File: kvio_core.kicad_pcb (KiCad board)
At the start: 6 copper layers, 60 x 41 mm, 196 parts, among them J1001 16-pin_FFC_(SFV16R), J1101 16-pin_FFC_(SFV16R), J1301 USB3_B_Micro, J401 16-pin_FFC_(SFV16R), J501 16-pin_FFC_(SFV16R), J601 16-pin_FFC_(SFV16R), J701 16-pin_FFC_(SFV16R), J801 16-pin_FFC_(SFV16R), J901 16-pin_FFC_(SFV16R), U1001 EMI8143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

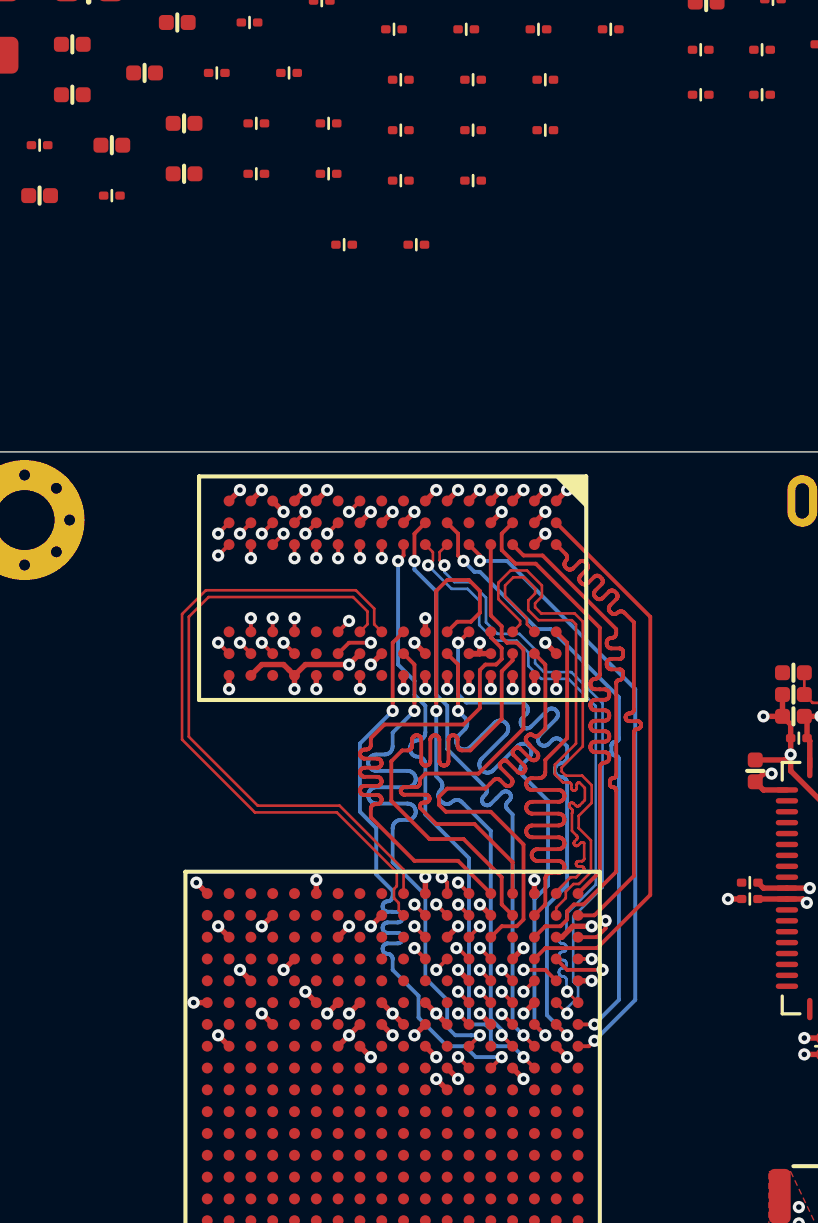
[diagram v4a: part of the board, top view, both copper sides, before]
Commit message: Cleaning up length tuning
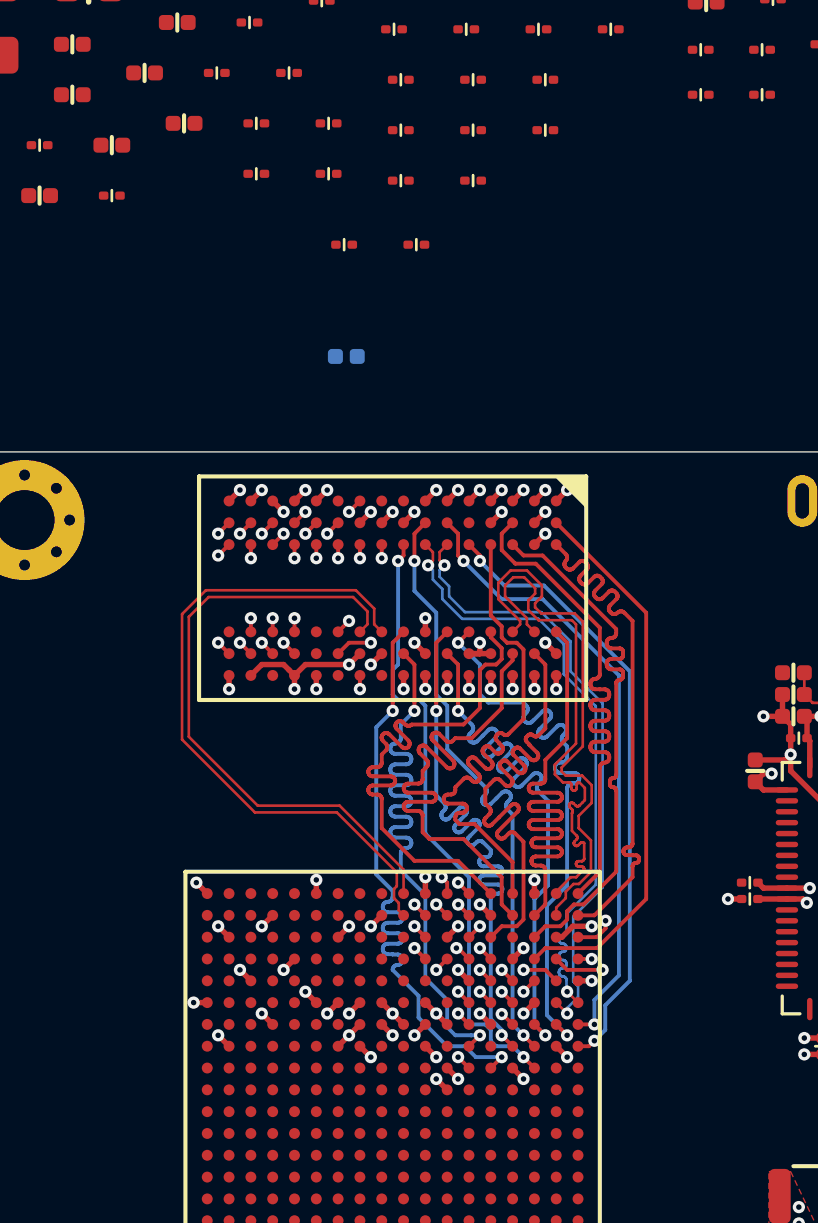
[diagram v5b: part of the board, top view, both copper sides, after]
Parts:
- C217: moved to B.Cu
- moved C217 8.96 mm to (183.3, 85.5)

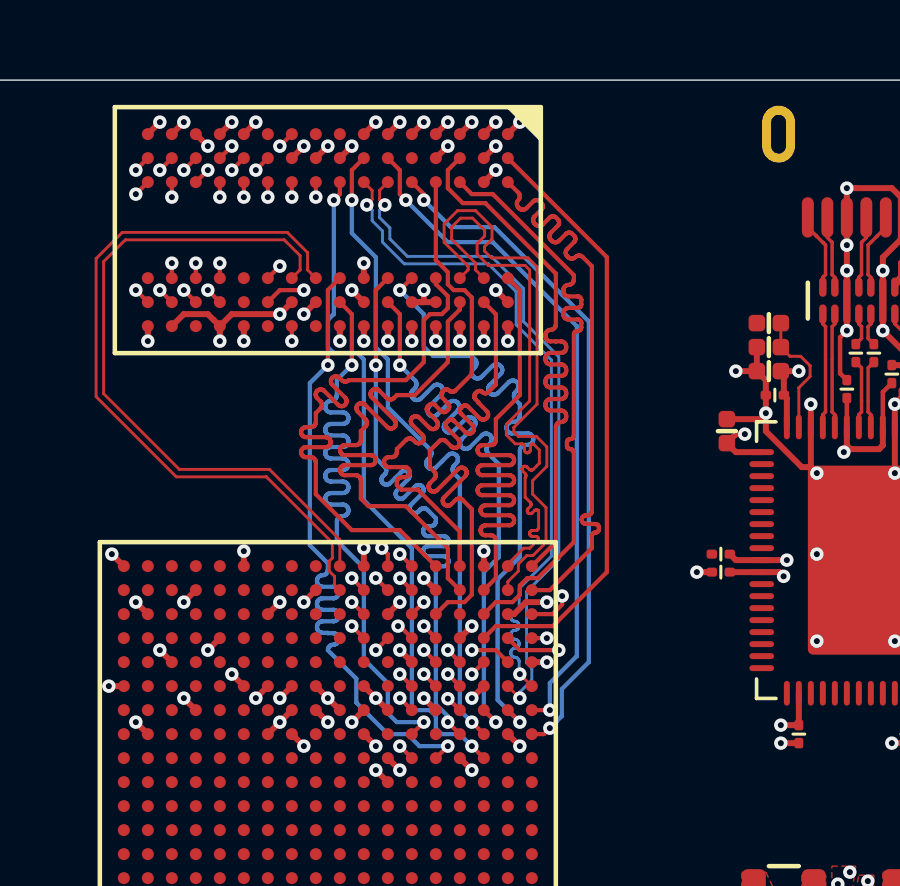
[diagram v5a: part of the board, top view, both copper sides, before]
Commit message: Fixing for adding pad lengths
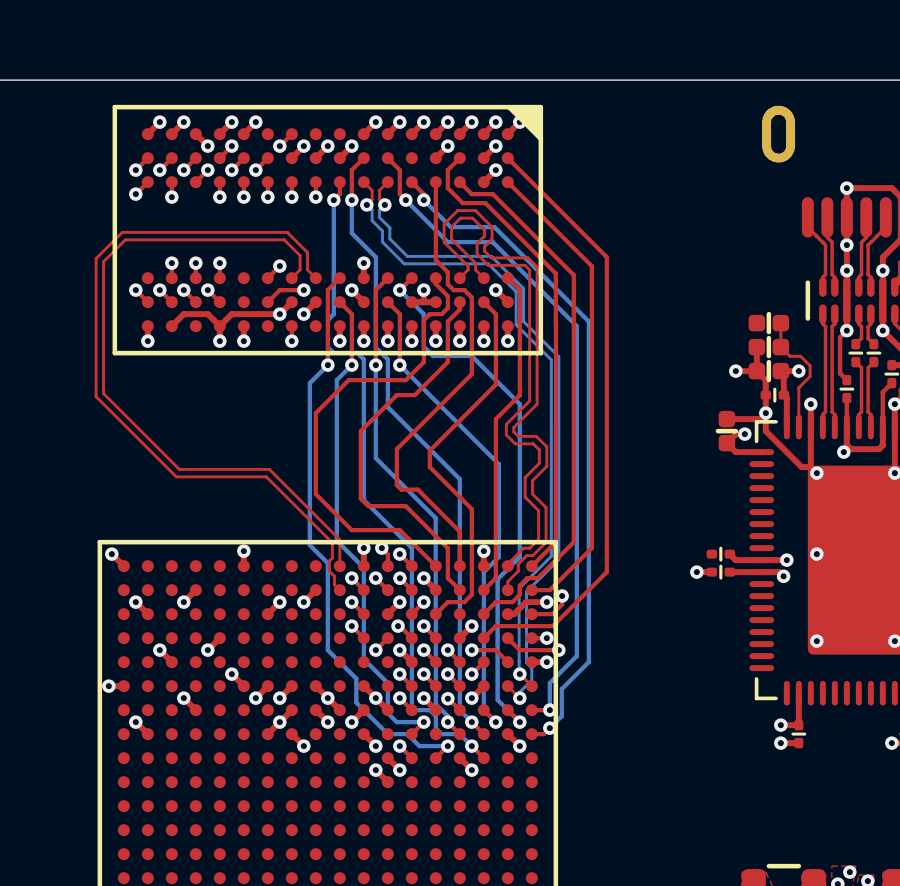
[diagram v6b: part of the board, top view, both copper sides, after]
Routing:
- net /DDR Memory/A4: track 26.2 -> 14.0 mm
- net /DDR Memory/BA1: track 26.2 -> 14.3 mm
- net /DDR Memory/A6: track 26.2 -> 15.8 mm
- net /DDR Memory/A1: track 26.2 -> 16.9 mm
- net /DDR Memory/DQ12: track 20.2 -> 11.1 mm
- net /DDR Memory/DQ14: track 20.2 -> 12.9 mm
- net /DDR Memory/A12: track 26.1 -> 19.2 mm
- net /DDR Memory/DQ10: track 20.2 -> 13.4 mm
- net /DDR Memory/A11: track 26.1 -> 20.0 mm
- net /DDR Memory/DQ3: track 22.6 -> 16.5 mm
- net /DDR Memory/DQ1: track 22.6 -> 16.5 mm
- net /DDR Memory/DQ5: track 22.6 -> 16.7 mm
- net /DDR Memory/A10: track 26.2 -> 21.5 mm
- net /DDR Memory/DQ8: track 20.2 -> 15.5 mm
- net /DDR Memory/UDM: track 20.2 -> 15.7 mm
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
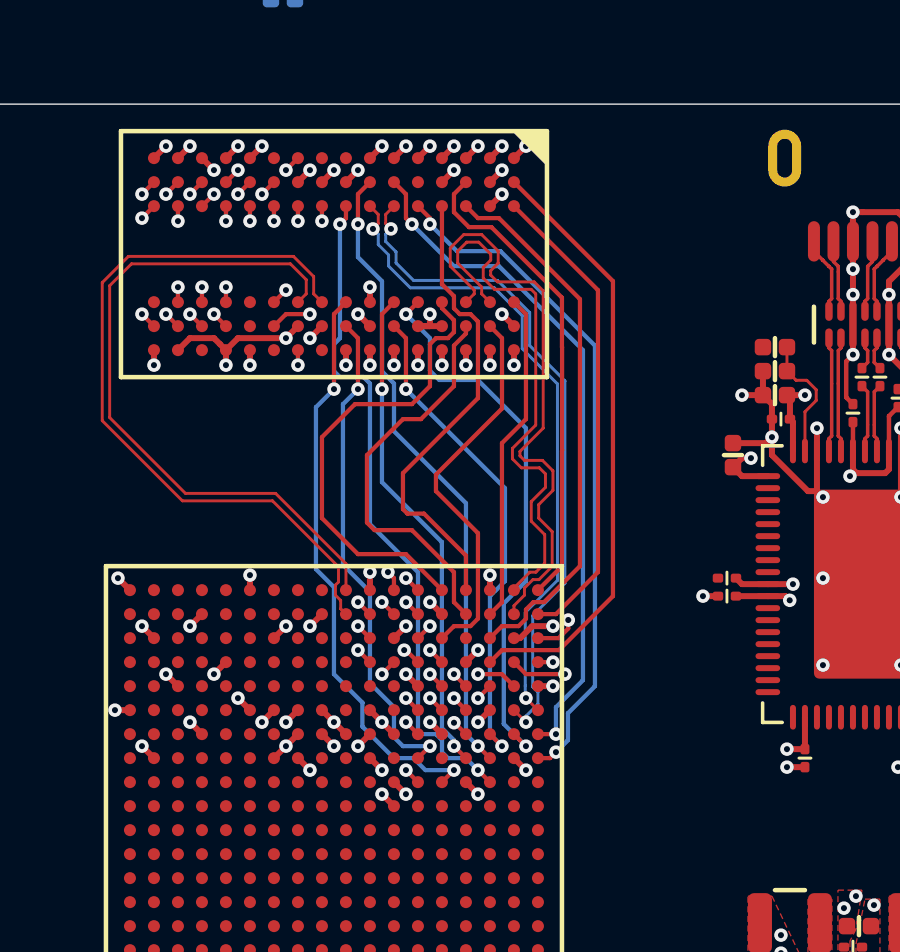
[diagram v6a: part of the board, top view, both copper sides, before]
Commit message: New length matching
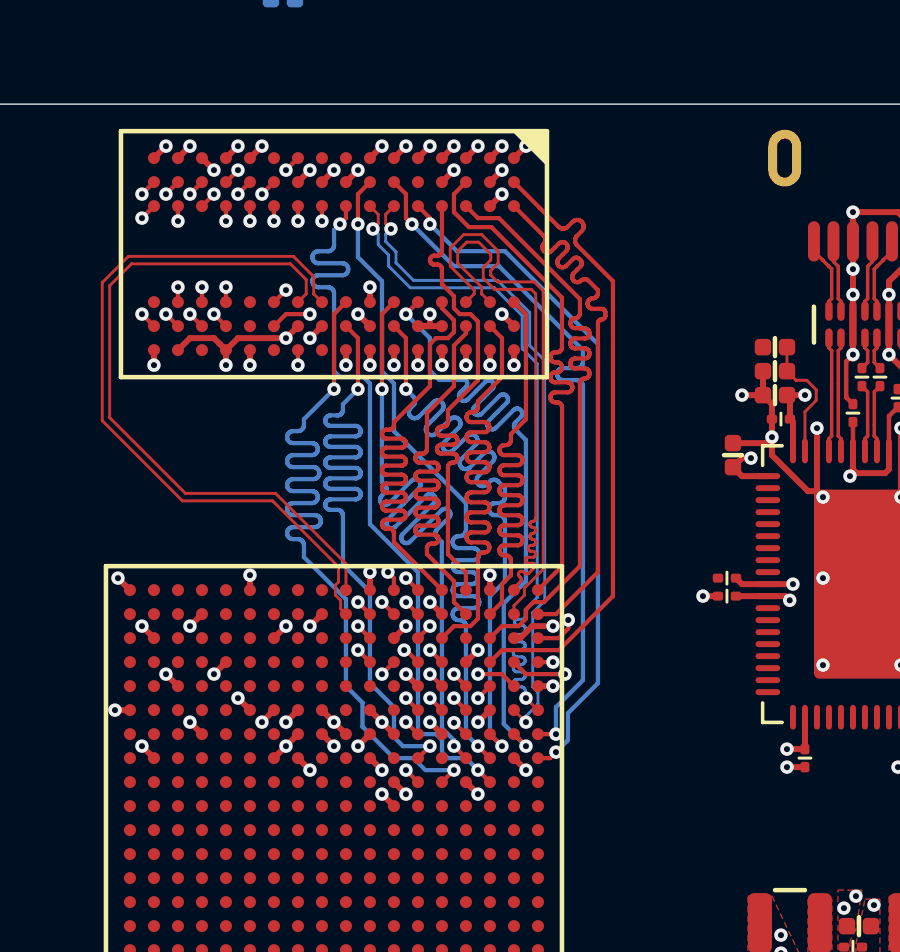
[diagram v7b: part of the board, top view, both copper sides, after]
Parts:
- U101: footprint bga:CSG324 -> bga:CSG324_Artix7_100T
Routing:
- net /DDR Memory/BA1: track 14.3 -> 25.5 mm
- net /DDR Memory/A4: track 14.0 -> 23.2 mm
- net /DDR Memory/DQ5: track 16.7 -> 25.8 mm
- net /DDR Memory/DQ1: track 16.5 -> 25.6 mm
- net /DDR Memory/A6: track 15.8 -> 24.6 mm
- net /DDR Memory/A11: track 20.0 -> 28.7 mm
- net /DDR Memory/DQ3: track 16.5 -> 25.1 mm
- net /DDR Memory/DQ7: track 19.4 -> 27.7 mm
- net /DDR Memory/DQ14: track 12.9 -> 20.2 mm
- net /DDR Memory/DQ12: track 11.1 -> 17.8 mm
- net /DDR Memory/A1: track 16.9 -> 23.5 mm
- net /DDR Memory/LDM: track 18.6 -> 24.4 mm
- net /DDR Memory/A10: track 21.5 -> 27.0 mm
- net /DDR Memory/A2: track 26.2 -> 20.9 mm
- net /DDR Memory/DQ6: track 21.2 -> 25.9 mm
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
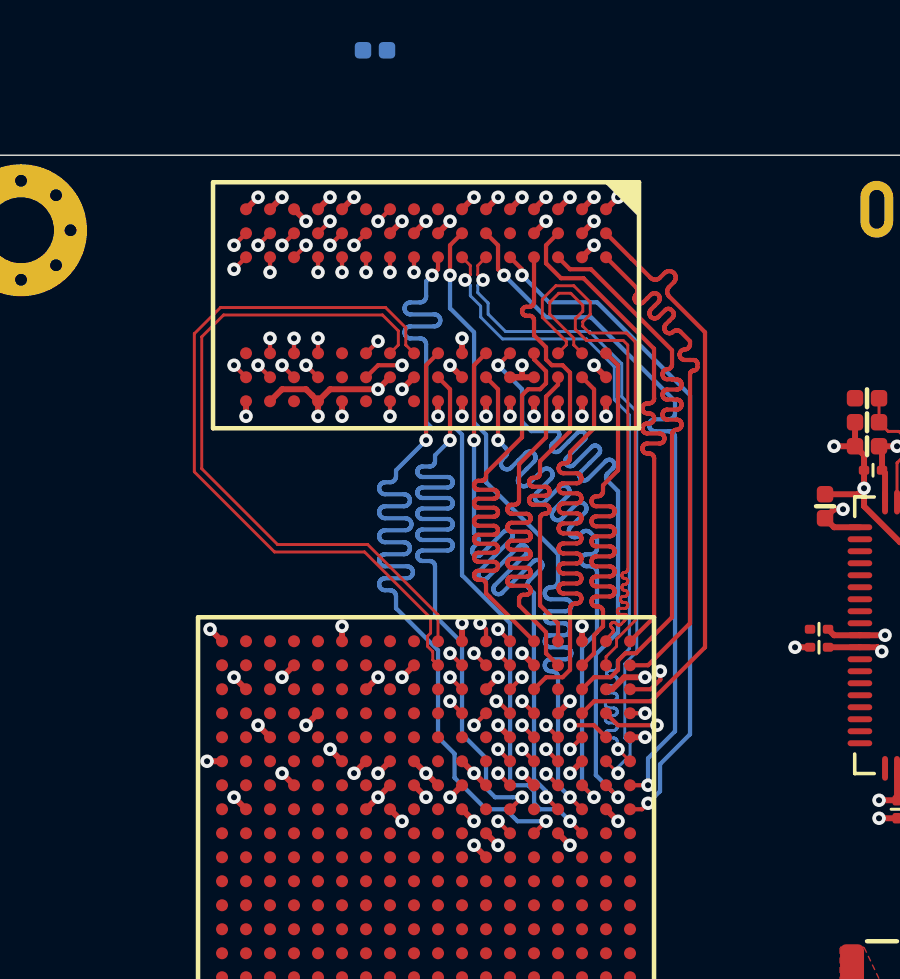
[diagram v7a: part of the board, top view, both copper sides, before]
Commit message: Now with DDR3 1.5 mm closer
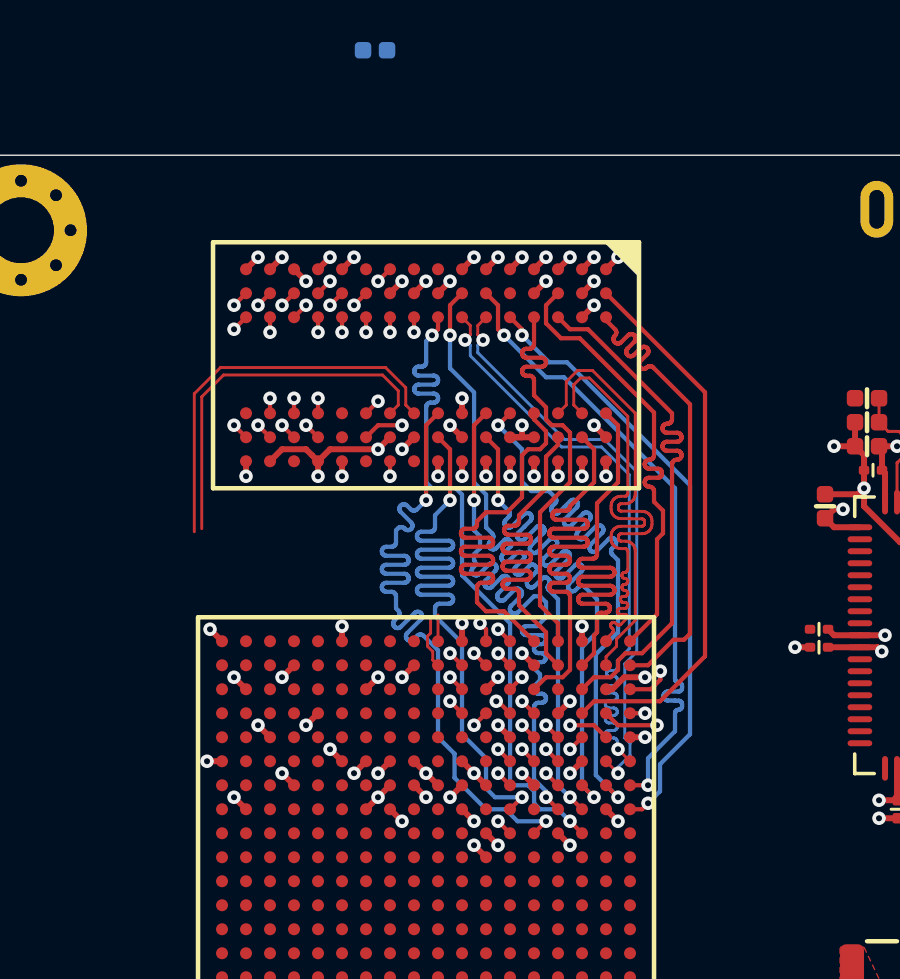
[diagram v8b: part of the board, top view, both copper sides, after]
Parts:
- moved U1201 2.00 mm to (185.0, 96.0)
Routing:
- net /DDR Memory/CK_N: track 23.1 -> 13.2 mm
- net /DDR Memory/CK_P: track 24.9 -> 15.0 mm
- net /DDR Memory/DQ9: track 21.0 -> 18.1 mm
- net /DDR Memory/LDQS_N: track 24.1 -> 21.3 mm
- net /DDR Memory/LDQS_P: track 22.3 -> 19.4 mm
- net /DDR Memory/DQ1: track 25.6 -> 22.8 mm
- net /DDR Memory/DQ13: track 21.1 -> 18.4 mm
- net /DDR Memory/DQ15: track 19.2 -> 16.5 mm
- net /DDR Memory/DQ11: track 18.2 -> 15.5 mm
- net /DDR Memory/UDM: track 16.8 -> 14.1 mm
- net /DDR Memory/DQ10: track 17.1 -> 14.3 mm
- net /DDR Memory/DQ14: track 20.2 -> 17.5 mm
- net /DDR Memory/DQ12: track 17.8 -> 15.1 mm
- net /DDR Memory/DQ8: track 18.7 -> 16.0 mm
- net /DDR Memory/UDQS_P: track 18.3 -> 15.6 mm
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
